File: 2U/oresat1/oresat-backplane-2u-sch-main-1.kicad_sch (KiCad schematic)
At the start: 22 parts

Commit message: Update of OreSat1 2U backplane. Removed extraneous connectors, imported DXF from OnShape and moved debug connectors by 0.176 mm. Routing left to do.
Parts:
- removed C7, C8: 10u 25V 0805, Capacitor_SMD:C_1206_3216Metric, symbol Device:C
- removed CF7.2, CF8.2: SFM-120-01-S-D-LC, oresat-connectors:J-SAMTEC-SFM-120-X1-XXX-D, symbol oresat-connectors:J-SAMTEC-SFM-120-X1-XXX-D
- C1.1, C1.2: footprint oresat-passives:0603-SMALL -> oresat-passives:0603-C-NOSILK

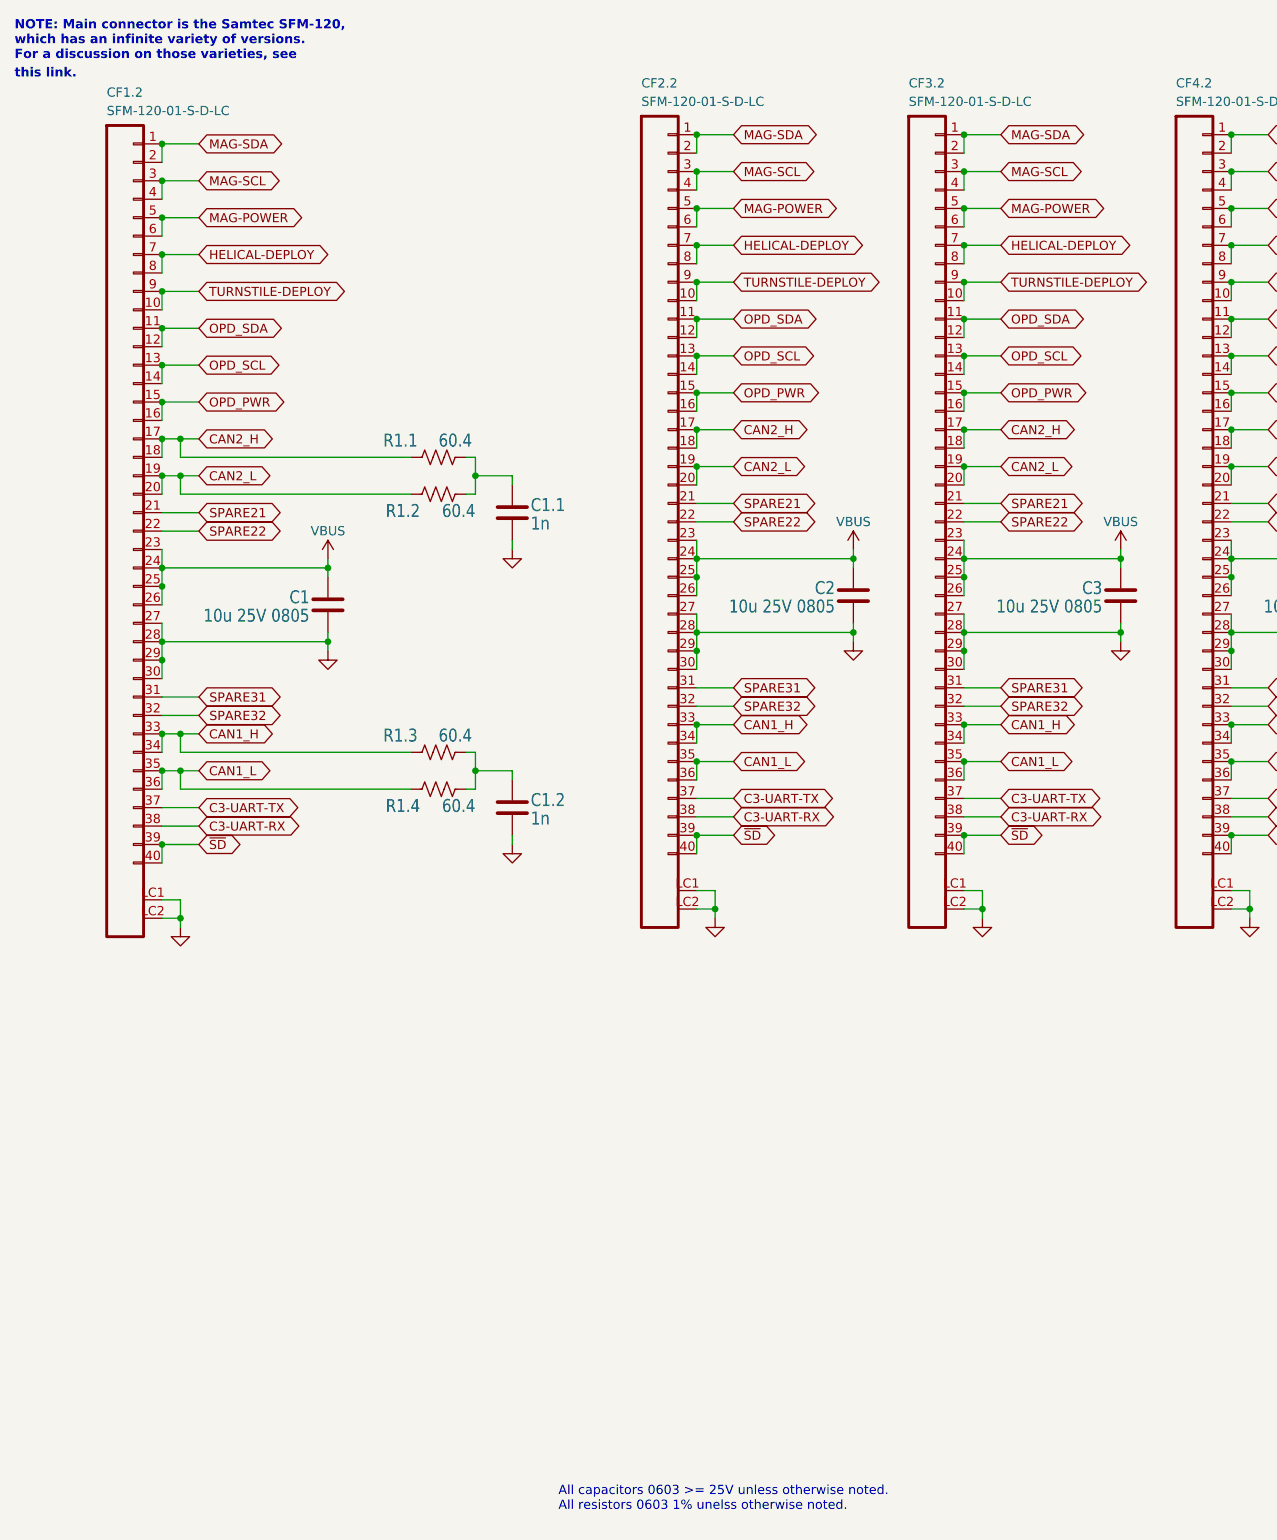
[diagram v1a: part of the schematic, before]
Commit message: Final fix and polish on 2U backplane for OreSat1.
Found a bunch of small little details to fix - somehow CAN lines were down to 0.2 mm, fixed to 0.3 mm. Also expanded some of
the lines to 0.6 mm for higher power lines. Added more vias for VBUS on the debug connector, and finally added 3D models
to all of the connectors so the backplane fully renders now!
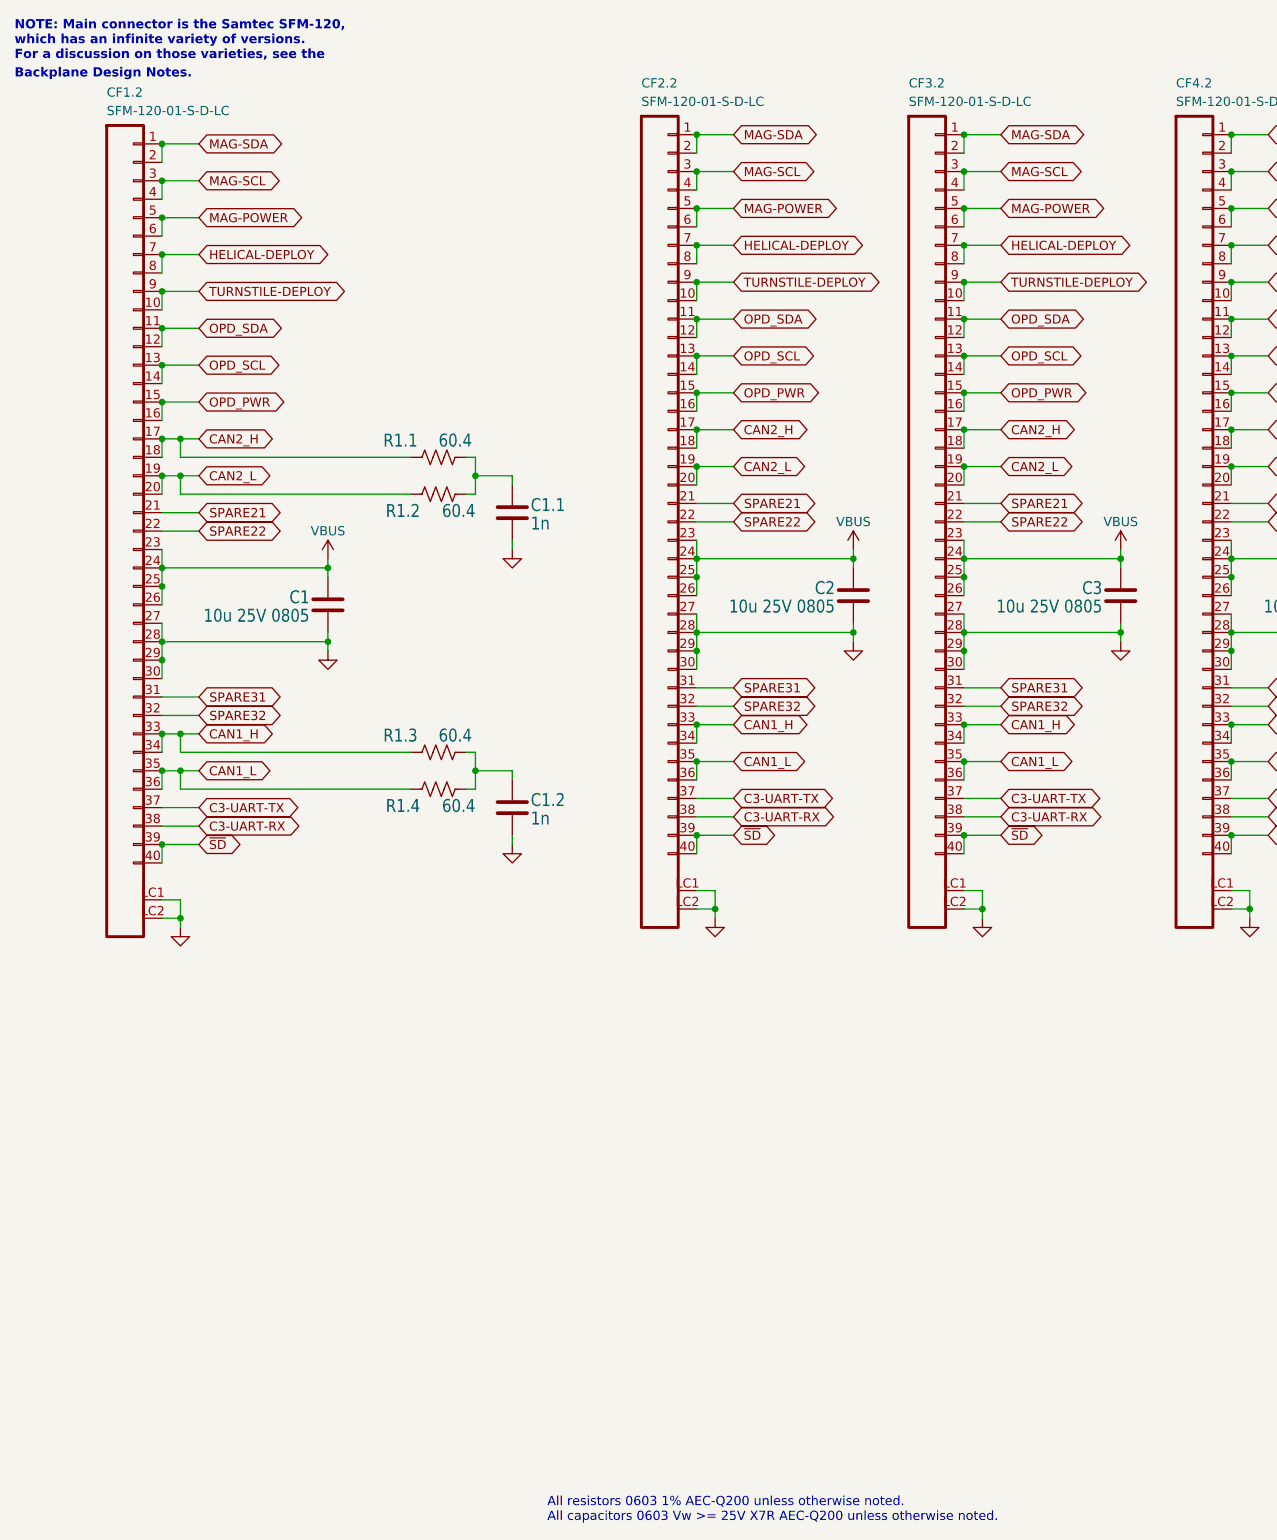
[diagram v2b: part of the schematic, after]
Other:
- note added: "All resistors 0603 1% AEC-Q200 unless otherwise noted. All capacitors 0603 Vw >= 25V X7R AEC-Q200 unless otherwise noted."
- note added: "Backplane Design Notes."
- note added: "NOTE: Main connector is the Samtec SFM-120, which has an infinite variety of versions. For a discussion on those varieties, see the"
- note removed: "All capacitors 0603 >= 25V unless otherwise noted. All resistors 0603 1% unelss otherwise noted."
- note removed: "NOTE: Main connector is the Samtec SFM-120, which has an infinite variety of versions. For a discussion on those varieties, see"
- note removed: "this link."
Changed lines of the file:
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@@
 	(title_block
 		(title "OreSat1 2U Backplane")
-		(date "2025-09-28")
+		(date "2025-11-30")
 		(rev "1.0")
 		(company "Portland State Aerospace Society")
 	)
-	(text "NOTE: Main connector is the Samtec SFM-120, \nwhich has an infinite variety of versions.\nFor a discussion on those varieties, see"
+	(text "NOTE: Main connector is the Samtec SFM-120, \nwhich has an infinite variety of versions.\nFor a discussion on those varieties, see the"
 		(exclude_from_sim no)
 		(at 40.64 64.77 0)
@@
 		)
 	)
-	(text "All capacitors 0603 >= 25V unless otherwise noted.\nAll resistors 0603 1% unelss otherwise noted."
+	(text "All resistors 0603 1% AEC-Q200 unless otherwise noted.\nAll capacitors 0603 Vw >= 25V X7R AEC-Q200 unless otherwise noted.\n"
 		(exclude_from_sim no)
-		(at 115.57 262.89 0)
+		(at 114.046 264.414 0)
 		(effects
 			(font
@@
 		)
 	)
-	(text "this link."
+	(text "Backplane Design Notes."
 		(exclude_from_sim no)
 		(at 40.64 67.31 0)

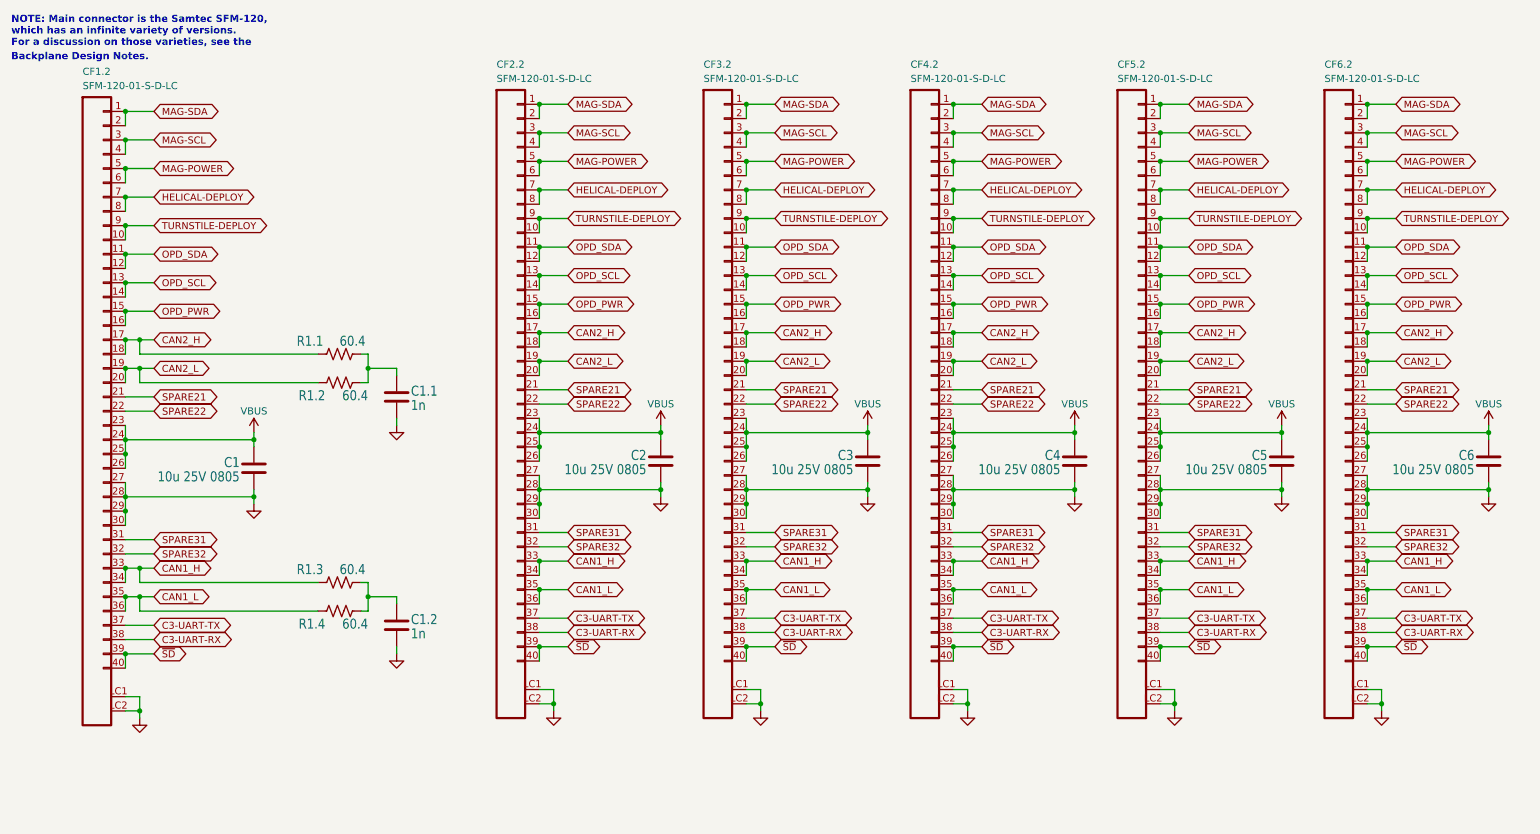
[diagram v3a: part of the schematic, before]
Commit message: Removed deployables and turned them into spares.
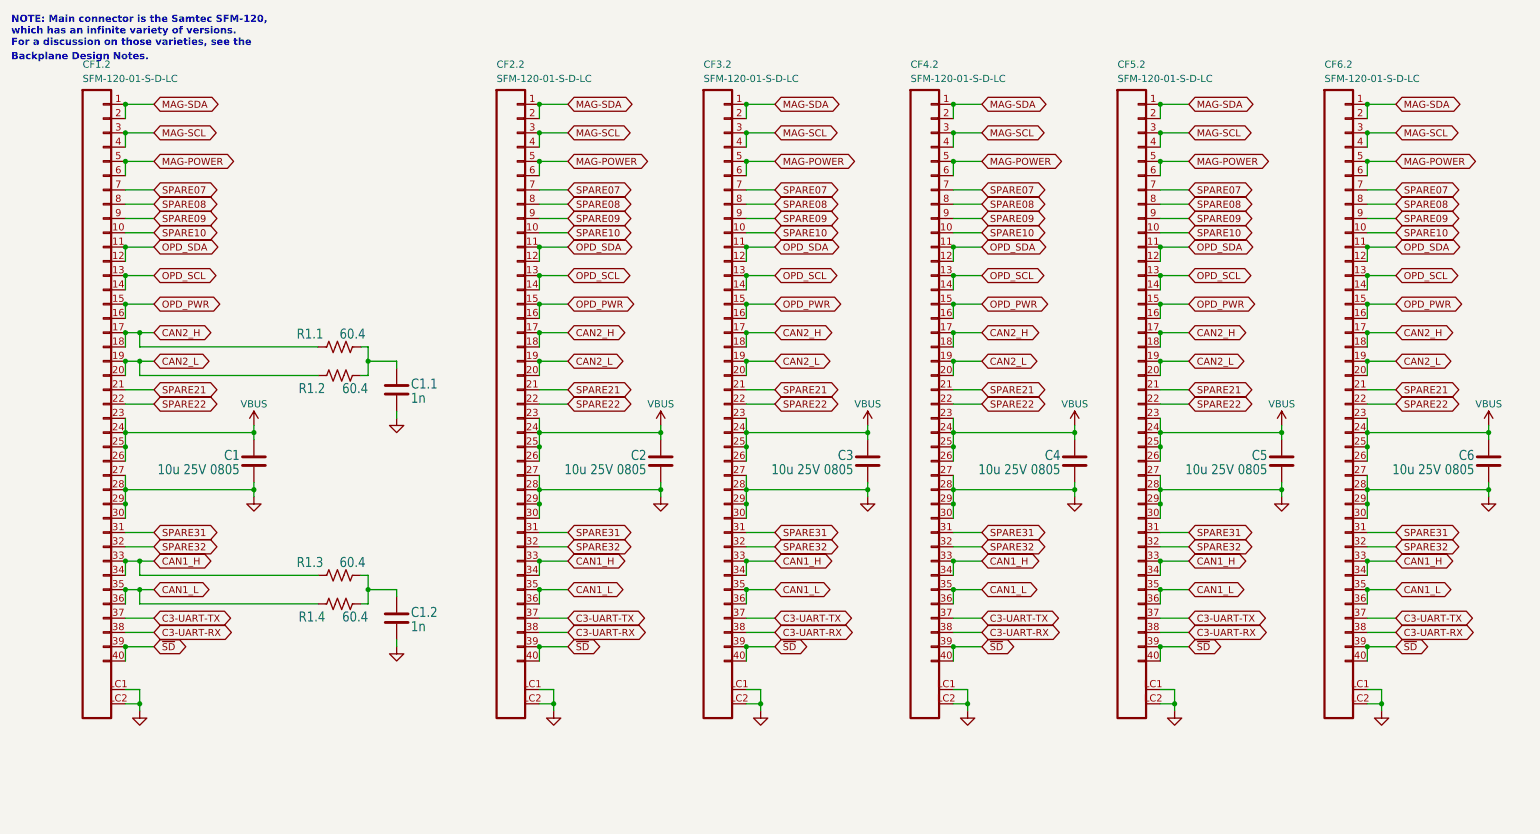
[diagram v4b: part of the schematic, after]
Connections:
- net HELICAL-DEPLOY renamed SPARE07
- net SPARE07: no longer CF1.2.8, CF2.2.8, CF3.2.8, CF4.2.8, CF5.2.8, CF6.2.8
- net TURNSTILE-DEPLOY renamed SPARE09
- net SPARE09: no longer CF1.2.10, CF2.2.10, CF3.2.10, CF4.2.10, CF5.2.10, CF6.2.10
- new net SPARE08: CF1.2.8, CF2.2.8, CF3.2.8, CF4.2.8, CF5.2.8, CF6.2.8
- new net SPARE10: CF1.2.10, CF2.2.10, CF3.2.10, CF4.2.10, CF5.2.10, CF6.2.10
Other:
- moved on the sheet: C1, C1.1, C1.2, CF1.2, R1.1, R1.2, R1.3, R1.4
